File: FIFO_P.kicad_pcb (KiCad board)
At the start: 4 copper layers, 100 x 100 mm, 77 parts, among them J1 Vin +, J2 Vin -, J3 ICLK, J4 Vout, J5 Jack-DC, M3 MountingHole_3.2mm_M3_ISO14580, M4 MountingHole_4.3mm_M4_Pad_Via, SW1 Rotary_Encoder_61C, U1 SN74LVC2G157_MUX_TI, U10 AD7840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

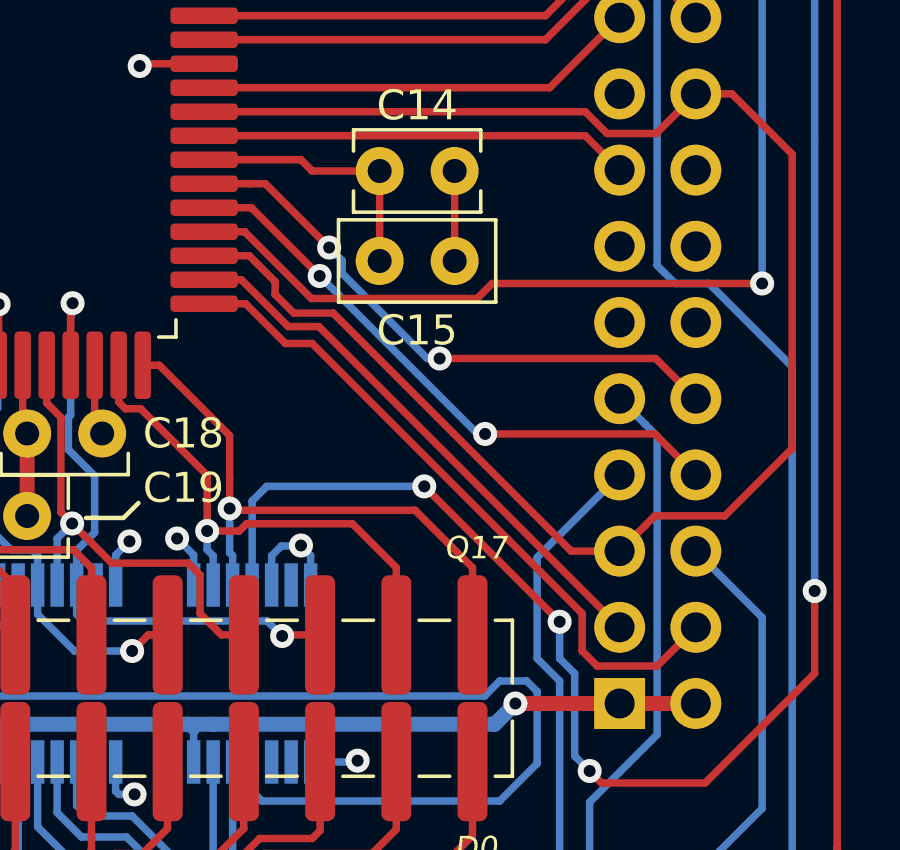
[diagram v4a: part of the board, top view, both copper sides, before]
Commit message: Swapped RT and OE to be sensible
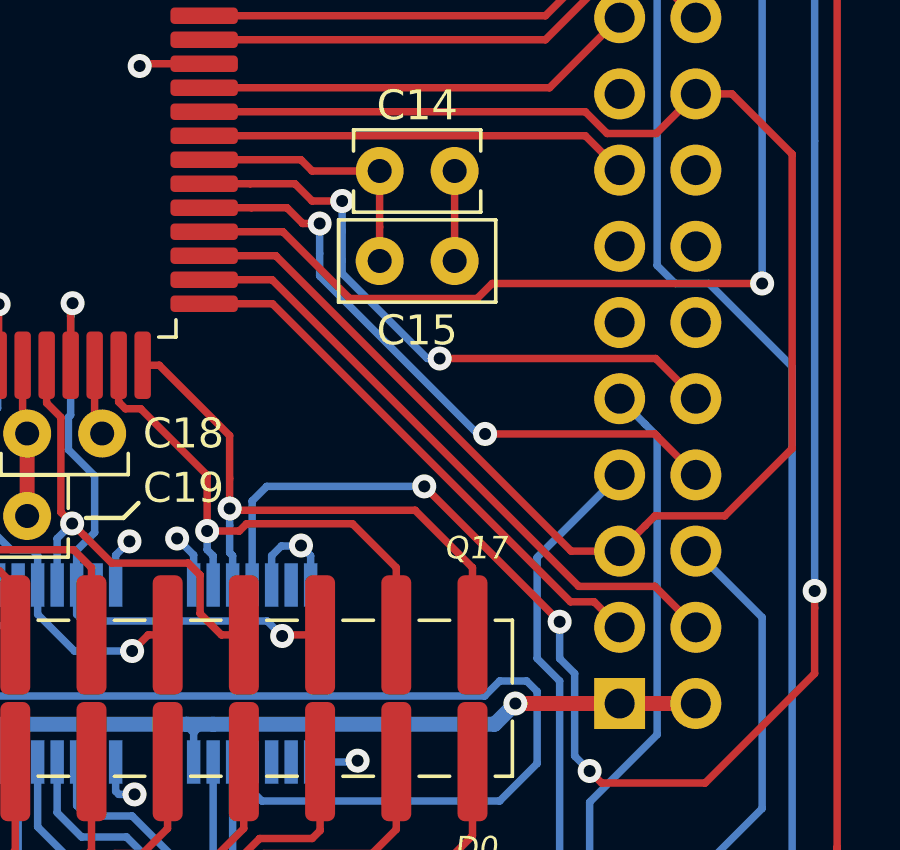
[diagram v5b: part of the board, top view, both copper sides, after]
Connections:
- U4 pad 22: Net-(U4-Pad22) -> Net-(U4-Pad23)
- U4 pad 23: Net-(U4-Pad23) -> Net-(U4-Pad22)
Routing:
- net Net-(U4-Pad23): track 22.7 -> 18.3 mm
- net Net-(U4-Pad22): track 21.0 -> 23.6 mm
- net Net-(U4-Pad29): track 19.6 -> 20.8 mm
- net Net-(U4-Pad27): track 20.3 -> 21.4 mm
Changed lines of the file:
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@@
     (thickness 1.6)
     (drawings 126)
-    (tracks 1159)
+    (tracks 1156)
     (zones 0)
     (modules 77)
@@
     (mod_text_size 1 1)
     (mod_text_width 0.15)
-    (pad_size 2.25 0.55)
-    (pad_drill 0)
+    (pad_size 1.7 1.7)
+    (pad_drill 1)
     (pad_to_mask_clearance 0)
     (aux_axis_origin 0 0)
@@
       (net 43 "Net-(U4-Pad24)"))
     (pad 23 thru_hole oval (at -2.54 -2.54) (size 1.7 1.7) (drill 1) (layers *.Cu *.Mask)
-      (net 44 "Net-(U4-Pad23)"))
-    (pad 22 thru_hole oval (at -2.54 0) (size 1.7 1.7) (drill 1) (layers *.Cu *.Mask)
       (net 45 "Net-(U4-Pad22)"))
+    (pad 22 thru_hole oval (at -2.54 0) (size 1.7 1.7) (drill 1) (layers *.Cu *.Mask)
+      (net 44 "Net-(U4-Pad23)"))
     (pad 5V thru_hole oval (at 0 -2.54) (size 1.7 1.7) (drill 1) (layers *.Cu *.Mask)
       (net 4 +5V))
@@
   (segment (start 130.75 71.5) (end 132.25 70) (width 0.25) (layer B.Cu) (net 24))
   (segment (start 132.25 70) (end 141.38641 70) (width 0.25) (layer B.Cu) (net 24))
-  (segment (start 126.999694 100.775) (end 125.65 100.775) (width 0.25) (layer F.Cu) (net 24))
-  (segment (start 129.224694 103) (end 126.999694 100.775) (width 0.25) (layer F.Cu) (net 24))
-  (segment (start 134.75 103) (end 129.224694 103) (width 0.25) (layer F.Cu) (net 24))
+  (segment (start 128.275 100.775) (end 125.65 100.775) (width 0.25) (layer F.Cu) (net 24))
+  (segment (start 130.5 103) (end 128.275 100.775) (width 0.25) (layer F.Cu) (net 24))
+  (segment (start 134.75 103) (end 130.5 103) (width 0.25) (layer F.Cu) (net 24))
   (segment (start 144.25 102.5) (end 135.25 102.5) (width 0.25) (layer F.Cu) (net 24))
   (segment (start 135.25 102.5) (end 134.75 103) (width 0.25) (layer F.Cu) (net 24))
@@
   (segment (start 138.355 97.575) (end 125.65 97.575) (width 0.25) (layer F.Cu) (net 40))
   (segment (start 139.5 98.72) (end 138.355 97.575) (width 0.25) (layer F.Cu) (net 40))
-  (segment (start 127.18641 99.175) (end 125.65 99.175) (width 0.25) (layer F.Cu) (net 41))
   (segment (start 142.04 106.34) (end 140.7 105) (width 0.25) (layer F.Cu) (net 41))
-  (via (at 129.816228 101.301315) (size 0.8) (drill 0.4) (layers F.Cu B.Cu) (net 41))
-  (segment (start 127.18641 99.175) (end 127.689913 99.175) (width 0.25) (layer F.Cu) (net 41))
-  (segment (start 127.689913 99.175) (end 129.816228 101.301315) (width 0.25) (layer F.Cu) (net 41))
   (segment (start 140.7 105) (end 133.5 105) (width 0.25) (layer F.Cu) (net 41))
   (via (at 133.5 105) (size 0.8) (drill 0.4) (layers F.Cu B.Cu) (net 41))
   (segment (start 133.084998 105) (end 133.5 105) (width 0.25) (layer B.Cu) (net 41))
   (segment (start 130.25 102.165002) (end 133.084998 105) (width 0.25) (layer B.Cu) (net 41))
-  (segment (start 129.816228 101.301315) (end 130.25 101.735087) (width 0.25) (layer B.Cu) (net 41))
   (segment (start 130.25 101.735087) (end 130.25 102.165002) (width 0.25) (layer B.Cu) (net 41))
-  (segment (start 127.225 99.975) (end 125.65 99.975) (width 0.25) (layer F.Cu) (net 42))
+  (segment (start 130.25 101.735087) (end 130.25 100.75) (width 0.25) (layer B.Cu) (net 41))
+  (segment (start 127.18641 99.175) (end 125.65 99.175) (width 0.25) (layer F.Cu) (net 41))
+  (segment (start 128.675 99.175) (end 127.18641 99.175) (width 0.25) (layer F.Cu) (net 41))
+  (via (at 130.25 99.75) (size 0.8) (drill 0.4) (layers F.Cu B.Cu) (net 41))
+  (segment (start 130.25 100.75) (end 130.25 99.75) (width 0.25) (layer B.Cu) (net 41))
+  (segment (start 129.25 99.75) (end 128.675 99.175) (width 0.25) (layer F.Cu) (net 41))
+  (segment (start 130.25 99.75) (end 129.25 99.75) (width 0.25) (layer F.Cu) (net 41))
   (segment (start 142.04 108.88) (end 140.675001 107.515001) (width 0.25) (layer F.Cu) (net 42))
-  (via (at 129.5 102.25) (size 0.8) (drill 0.4) (layers F.Cu B.Cu) (net 42))
-  (segment (start 127.225 99.975) (end 129.5 102.25) (width 0.25) (layer F.Cu) (net 42))
   (via (at 135.015001 107.515001) (size 0.8) (drill 0.4) (layers F.Cu B.Cu) (net 42))
   (segment (start 134.765001 107.515001) (end 135.015001 107.515001) (width 0.25) (layer B.Cu) (net 42))
@@
   (segment (start 140.675001 107.515001) (end 135.015001 107.515001) (width 0.25) (layer F.Cu) (net 42))
   (segment (start 135.015001 107.515001) (end 134.765001 107.515001) (width 0.25) (layer F.Cu) (net 42))
+  (segment (start 129.5 102.25) (end 129.5 101.5) (width 0.25) (layer B.Cu) (net 42))
+  (via (at 129.5 100.5) (size 0.8) (drill 0.4) (layers F.Cu B.Cu) (net 42))
+  (segment (start 129.5 101.5) (end 129.5 100.5) (width 0.25) (layer B.Cu) (net 42))
+  (segment (start 127.225 99.975) (end 125.65 99.975) (width 0.25) (layer F.Cu) (net 42))
+  (segment (start 128.409315 99.975) (end 127.225 99.975) (width 0.25) (layer F.Cu) (net 42))
+  (segment (start 128.934315 100.5) (end 128.409315 99.975) (width 0.25) (layer F.Cu) (net 42))
+  (segment (start 129.5 100.5) (end 128.934315 100.5) (width 0.25) (layer F.Cu) (net 42))
   (segment (start 125.275 96.775) (end 125.879088 96.775) (width 0.25) (layer F.Cu) (net 43))
-  (segment (start 127.1545 101.575) (end 128.015 102.4355) (width 0.25) (layer F.Cu) (net 43))
-  (segment (start 125.65 101.575) (end 127.1545 101.575) (width 0.25) (layer F.Cu) (net 43))
-  (segment (start 137.883206 111.42) (end 139.5 111.42) (width 0.25) (layer F.Cu) (net 43))
-  (segment (start 128.015 102.863308) (end 128.639346 103.487654) (width 0.25) (layer F.Cu) (net 43))
-  (segment (start 128.015 102.4355) (end 128.015 102.863308) (width 0.25) (layer F.Cu) (net 43))
-  (segment (start 128.639346 103.487654) (end 129.95086 103.487654) (width 0.25) (layer F.Cu) (net 43))
-  (segment (start 129.95086 103.487654) (end 137.883206 111.42) (width 0.25) (layer F.Cu) (net 43))
   (segment (start 138.355998 96.775) (end 125.65 96.775) (width 0.25) (layer F.Cu) (net 43))
   (segment (start 139.080998 97.5) (end 138.355998 96.775) (width 0.25) (layer F.Cu) (net 43))
@@
   (segment (start 143.005001 110.244999) (end 140.675001 110.244999) (width 0.25) (layer F.Cu) (net 43))
   (segment (start 140.675001 110.244999) (end 140.349999 110.570001) (width 0.25) (layer F.Cu) (net 43))
-  (segment (start 140.75 115.25) (end 138.75 115.25) (width 0.25) (layer F.Cu) (net 44))
-  (segment (start 142.04 113.96) (end 140.75 115.25) (width 0.25) (layer F.Cu) (net 44))
-  (segment (start 138.75 115.25) (end 138.25 114.75) (width 0.25) (layer F.Cu) (net 44))
-  (segment (start 138.25 114.75) (end 138.25 113.5) (width 0.25) (layer F.Cu) (net 44))
-  (segment (start 138.25 113.5) (end 129.25 104.5) (width 0.25) (layer F.Cu) (net 44))
-  (segment (start 129.25 104.5) (end 128.359 104.5) (width 0.25) (layer F.Cu) (net 44))
-  (segment (start 127.034 103.175) (end 125.65 103.175) (width 0.25) (layer F.Cu) (net 44))
-  (segment (start 128.359 104.5) (end 127.034 103.175) (width 0.25) (layer F.Cu) (net 44))
+  (segment (start 137.883206 111.42) (end 139.5 111.42) (width 0.25) (layer F.Cu) (net 43))
+  (segment (start 125.65 101.575) (end 128.038206 101.575) (width 0.25) (layer F.Cu) (net 43))
+  (segment (start 128.038206 101.575) (end 137.883206 111.42) (width 0.25) (layer F.Cu) (net 43))
+  (segment (start 138.650001 113.110001) (end 139.5 113.96) (width 0.25) (layer F.Cu) (net 44))
+  (segment (start 137.860001 113.110001) (end 138.650001 113.110001) (width 0.25) (layer F.Cu) (net 44))
+  (segment (start 125.65 103.175) (end 127.925 103.175) (width 0.25) (layer F.Cu) (net 44))
+  (segment (start 127.925 103.175) (end 137.860001 113.110001) (width 0.25) (layer F.Cu) (net 44))
   (segment (start 125.275 102.375) (end 126.645294 102.375) (width 0.25) (layer F.Cu) (net 45))
   (segment (start 126.645294 102.375) (end 125.65 102.375) (width 0.25) (layer F.Cu) (net 45))
-  (segment (start 129.54 104) (end 139.5 113.96) (width 0.25) (layer F.Cu) (net 45))
-  (segment (start 129.477664 103.937664) (end 129.54 104) (width 0.25) (layer F.Cu) (net 45))
-  (segment (start 128.452946 103.937664) (end 129.477664 103.937664) (width 0.25) (layer F.Cu) (net 45))
-  (segment (start 126.890282 102.375) (end 128.452946 103.937664) (width 0.25) (layer F.Cu) (net 45))
-  (segment (start 125.65 102.375) (end 126.890282 102.375) (width 0.25) (layer F.Cu) (net 45))
+  (segment (start 140.675001 112.595001) (end 142.04 113.96) (width 0.25) (layer F.Cu) (net 45))
+  (segment (start 138.135001 112.595001) (end 140.675001 112.595001) (width 0.25) (layer F.Cu) (net 45))
+  (segment (start 125.65 102.375) (end 127.915 102.375) (width 0.25) (layer F.Cu) (net 45))
+  (segment (start 127.915 102.375) (end 138.135001 112.595001) (width 0.25) (layer F.Cu) (net 45))
   (segment (start 139.5 78.4) (end 139.35 78.4) (width 0.25) (layer F.Cu) (net 46))
   (segment (start 139.5 78.4) (end 140.675001 79.575001) (width 0.25) (layer F.Cu) (net 46))

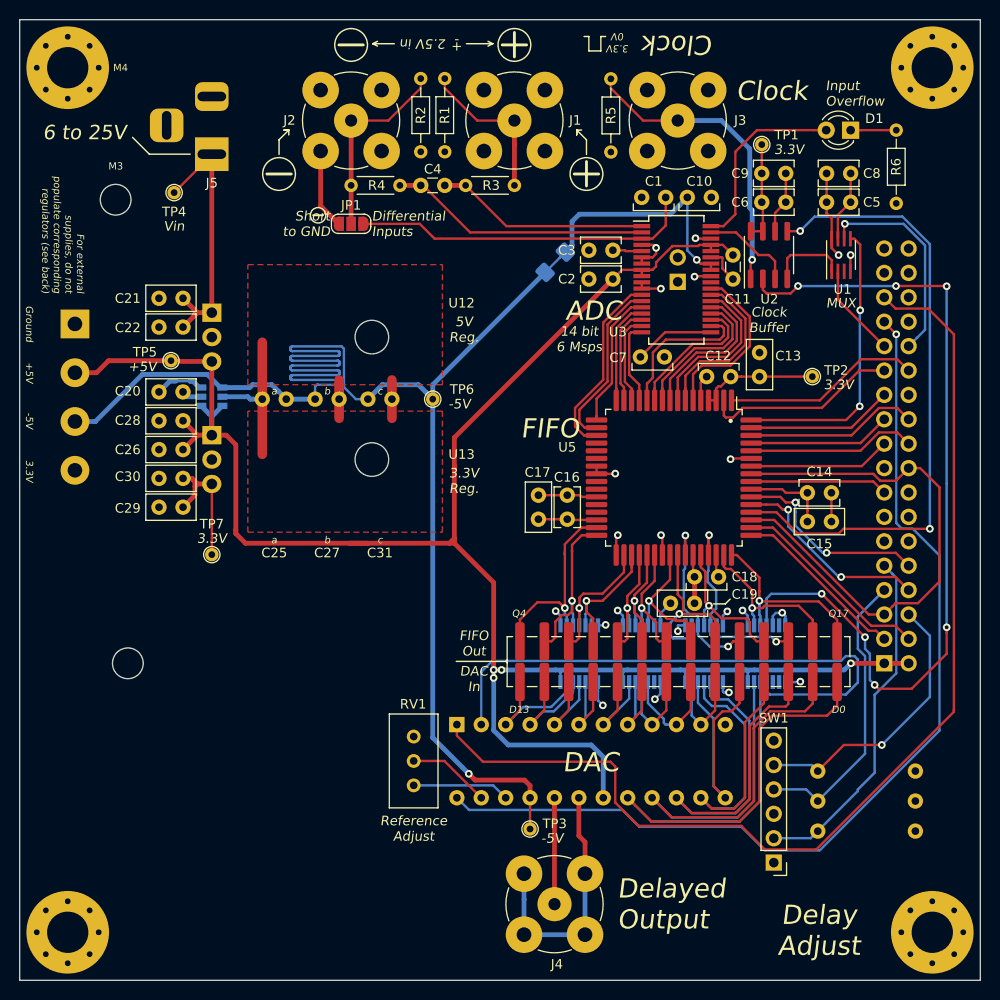
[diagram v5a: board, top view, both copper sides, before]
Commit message: Routed SMT DAC
Modified from after Edgar's changes
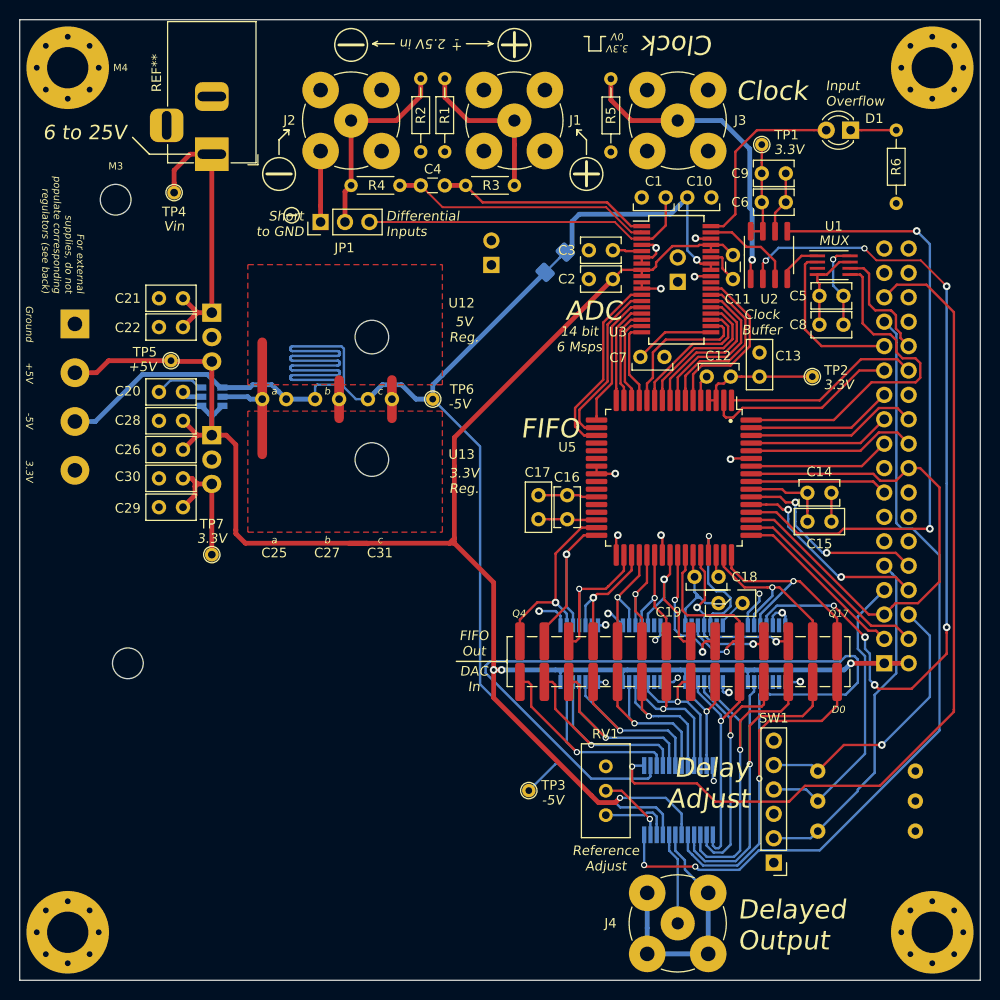
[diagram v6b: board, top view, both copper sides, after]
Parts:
- removed J5: Jack-DC, Connector_BarrelJack:BarrelJack_Horizontal
- added JP2: Jumper, Connector_PinHeader_2.54mm:PinHeader_1x02_P2.54mm_Vertical, F.Cu at (98.6, 75.0)
- added REF**: BarrelJack_Horizontal, Connector_BarrelJack:BarrelJack_Horizontal, F.Cu at (69.5, 63.5)
- JP1: footprint Jumper:SolderJumper-3_P1.3mm_Open_RoundedPad1.0x1.5mm -> Pin_Headers:Pin_Header_Straight_1x03_Pitch2.54mm
- U10: footprint Package_DIP:DIP-24_W7.62mm -> Package_SO:SSOP-24_5.3x8.2mm_P0.65mm
- moved U10 24.4 mm to (118.1, 130.8)
- moved RV1 20.2 mm to (110.5, 132.3)
- moved C8 16.1 mm to (132.8, 81.2), turned to 0 degrees
- moved J4 13.0 mm to (118.0, 143.6)
- moved C5 10.3 mm to (132.8, 78.2), turned to 0 degrees
- moved C19 7.50 mm to (124.8, 110.2), turned to 180 degrees
- moved TP3 4.00 mm to (102.5, 129.8)
- moved JP1 3.18 mm to (80.8, 70.6), turned to 90 degrees
- moved U1 1.30 mm to (134.2, 75.1), turned to 0 degrees
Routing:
- net Net-(U10-Pad1): track 114.3 -> 91.9 mm, vias 0 -> 1
- net Net-(U10-Pad17): track 62.9 -> 44.2 mm, vias 0 -> 1
- net LDAC5V: track 59.0 -> 76.5 mm
- net Net-(U10-Pad24): track 103.3 -> 85.8 mm, vias 1 -> 2
- net Net-(U10-Pad16): track 53.8 -> 39.9 mm, vias 0 -> 1
- net Net-(U10-Pad4): track 12.0 -> 25.7 mm, vias 0 -> 1
- net Net-(U10-Pad3): track 13.8 -> 27.6 mm, vias 0 -> 1
- net Net-(U10-Pad5): track 10.6 -> 24.0 mm, vias 0 -> 1
- net Net-(U10-Pad6): track 10.0 -> 21.7 mm, vias 0 -> 1
- net -5V: track 190.8 -> 202.0 mm, vias 2 -> 1
- net Net-(U10-Pad15): track 47.4 -> 36.2 mm, vias 0 -> 1
- net WLSTN: track 22.1 -> 12.9 mm, vias 1 -> 0
- net 3.3V: track 91.7 -> 100.4 mm, vias 9 -> 8
- net Net-(U10-Pad14): track 38.6 -> 30.5 mm, vias 0 -> 1
- net Net-(U10-Pad7): track 10.6 -> 18.3 mm, vias 0 -> 1
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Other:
- net class Default: via_dia 0.8 -> 0.65
- board text removed: "D13"
